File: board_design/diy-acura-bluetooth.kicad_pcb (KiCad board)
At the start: 2 copper layers, 127 x 76.2 mm, 40 parts, among them P1 MBUS_CONN, P2 CONN_01X03, Q1 2N3904, Q2 IRFU9024NPBF, Q3 2N3904, Q4 2N3904, U1 TLV2362, U2 AS393P-E1, U3 R-78E5.0-0.5, U4 TEENSY-3.2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

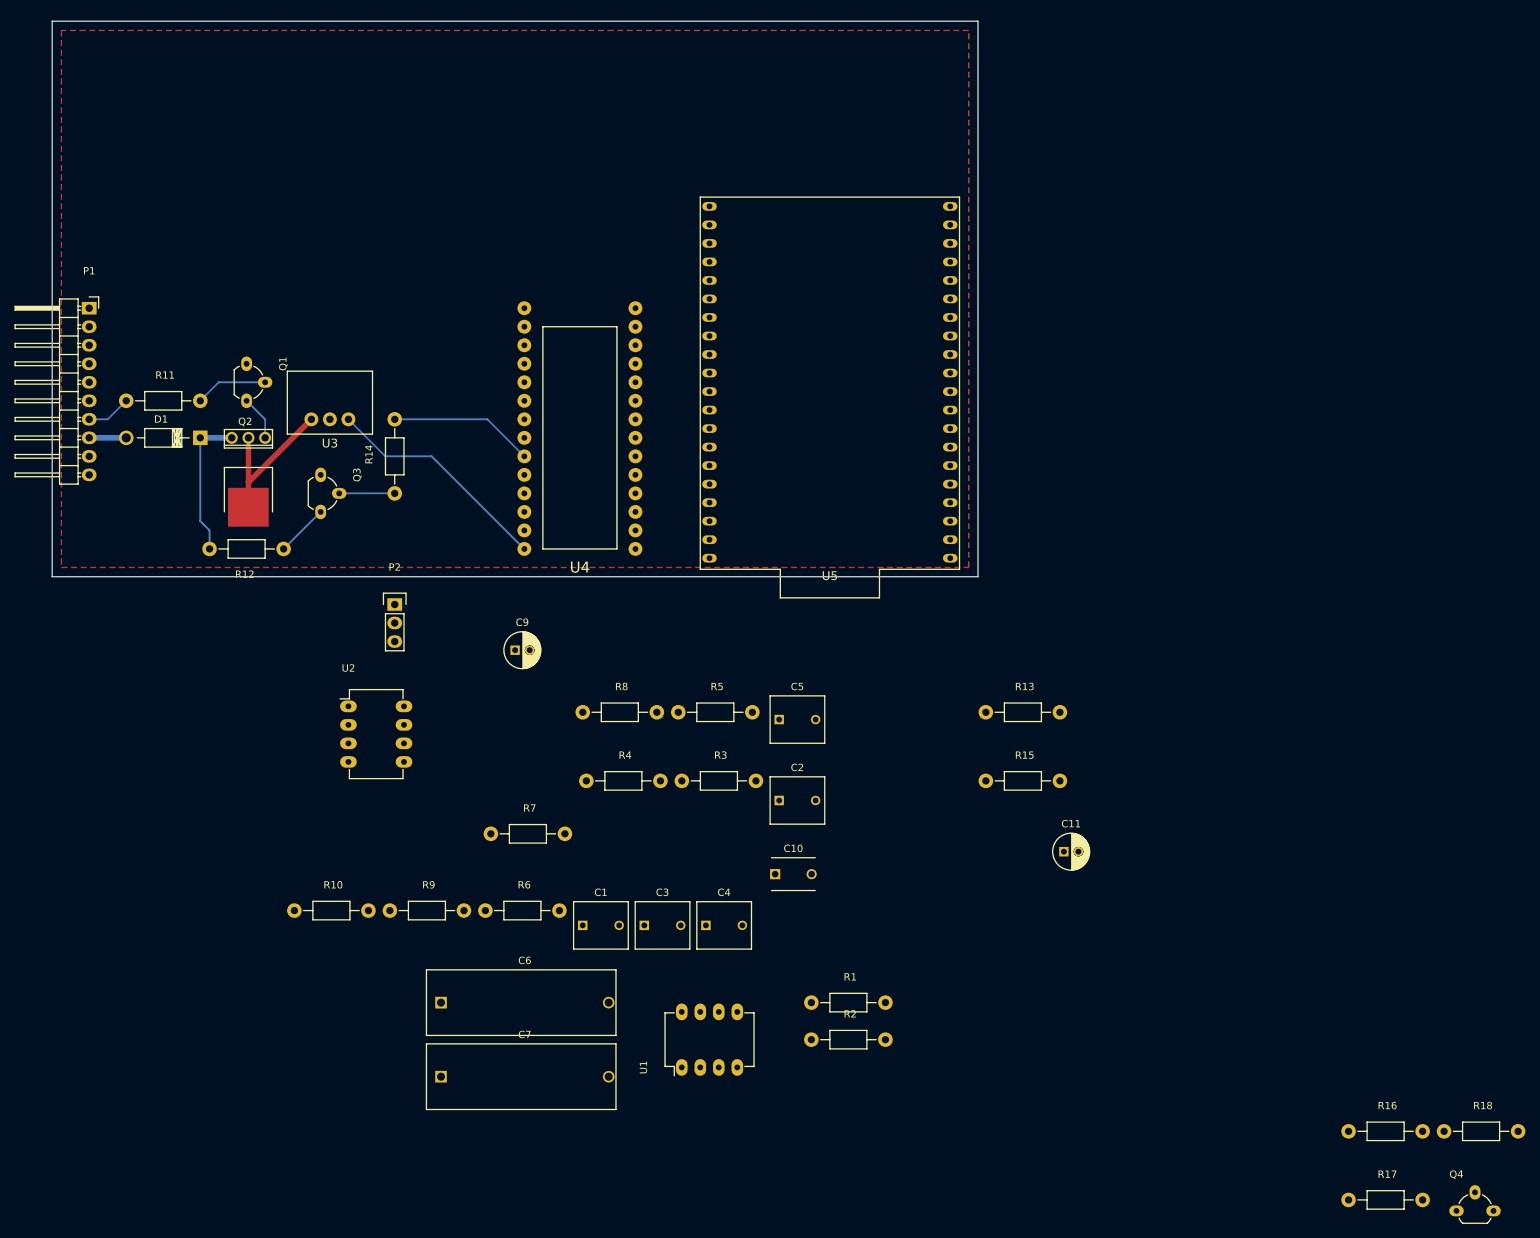
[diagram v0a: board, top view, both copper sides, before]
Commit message: WIP commit before redoing layout for 0.5mm bit and before adding microphone port.
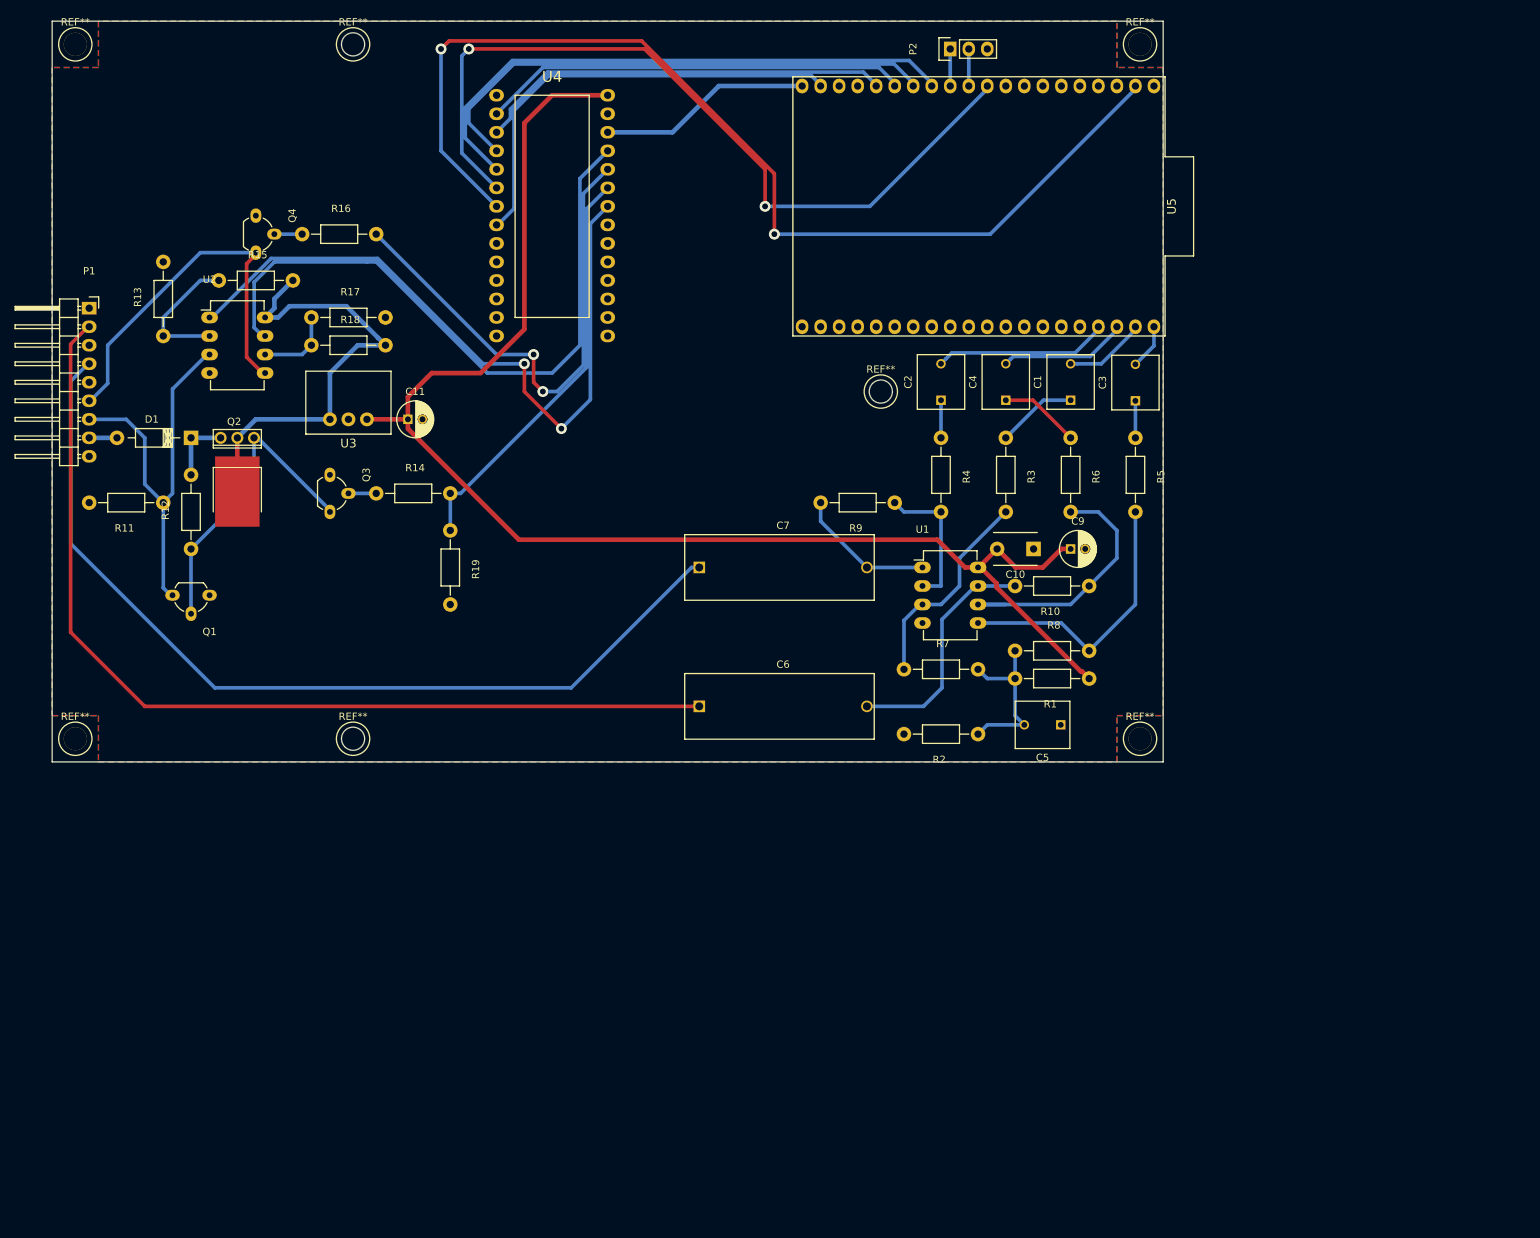
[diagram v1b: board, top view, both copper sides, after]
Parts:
- added R19: 4.75K, Resistors_ThroughHole:Resistor_Horizontal_RM10mm, F.Cu at (80.0, 95.2)
- added REF**: 1pin, Connect:1pin, F.Cu at (139.1, 76.2)
- added REF**: 1pin, Connect:1pin, F.Cu at (66.7, 123.8)
- added REF**: 1pin, Connect:1pin, F.Cu at (66.7, 28.6)
- added REF**: 1pin, Connect:1pin, F.Cu at (174.6, 28.6)
- added REF**: 1pin, Connect:1pin, F.Cu at (174.6, 123.8)
- added REF**: 1pin, Connect:1pin, F.Cu at (28.6, 123.8)
- added REF**: 1pin, Connect:1pin, F.Cu at (28.6, 28.6)
- Q1: value 2N3904 -> 5LN01SP
- R11: value 4.75K -> 47.5K
- moved Q4 213.9 mm to (53.3, 52.1), turned to 270 degrees
- moved R18 189.1 mm to (61.0, 69.8)
- moved R16 189.1 mm to (59.7, 54.6)
- moved R17 186.8 mm to (61.0, 66.0)
- moved R15 125.6 mm to (48.3, 61.0)
- moved R13 124.1 mm to (40.6, 68.6), turned to 90 degrees
- moved R10 117.8 mm to (167.6, 102.9), turned to 180 degrees
- moved P2 107.8 mm to (148.6, 29.2), turned to 90 degrees
- moved C11 107.8 mm to (74.2, 80.0)
- moved R6 103.2 mm to (165.1, 82.5), turned to 270 degrees
- moved C3 98.6 mm to (174.0, 77.5), turned to 90 degrees
- moved C1 98.3 mm to (165.1, 77.4), turned to 90 degrees
- moved R9 89.0 mm to (141.0, 91.4), turned to 180 degrees
- moved C4 83.0 mm to (156.2, 77.4), turned to 90 degrees
- moved C7 78.3 mm to (114.2, 100.3)
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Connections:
- net /bluetooth/3vIn renamed +3V3
- Q1 pad 3: Net-(Q1-Pad3) -> /power/accIn
- Q2 pad 1: Net-(Q1-Pad3) -> Net-(Q1-Pad2)
- Q3 pad 3: Net-(Q1-Pad3) -> Net-(Q1-Pad2)
- R11 pad 2: Net-(Q1-Pad2) -> GND
- R12 pad 1: Net-(Q1-Pad3) -> Net-(Q1-Pad2)
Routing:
- net +5V: track 31.5 -> 194.9 mm
- net /bluetooth/connStatEventOut: track 0.00 -> 145.0 mm, vias 0 -> 2
- net /audio/left: track 0.00 -> 133.5 mm
- net /audio/right: track 0.00 -> 127.1 mm
- net /bluetooth/cmdLoIn: track 0.00 -> 111.5 mm, vias 0 -> 2
- net /teensy/accSenseIn: track 0.00 -> 97.0 mm, vias 0 -> 2
- net /teensy/mbusSenseIn: track 0.00 -> 90.2 mm
- net /teensy/rn52RtsIn: track 0.00 -> 78.6 mm
- net /teensy/rn52CtsOut: track 0.00 -> 72.3 mm
- net /mbus_if/driveMbusLoIn: track 0.00 -> 69.3 mm, vias 0 -> 2
- net /bluetooth/powerEnIn: track 0.00 -> 61.5 mm
- net /teensy/rn52RxIn: track 0.00 -> 58.5 mm
- net /teensy/rn52TxOut: track 0.00 -> 57.7 mm
- net /mbus_if/mbusBi: track 0.00 -> 52.6 mm
- net /power/accIn: track 6.13 -> 55.3 mm
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- added copper zone on B.Cu, net GND
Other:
- board size 127 x 76.2 mm -> 152.4 x 101.6 mm
- net class Default: clearance 0.2 -> 0.52; trace_width 0.25 -> 0.5
- net class power added: clearance 0.52, trace_width 0.635, via_dia 0.6, via_drill 0.4
- rule trace_clearance: 0.2 -> 0.52
- rule trace_min: 0.2 -> 0.5
